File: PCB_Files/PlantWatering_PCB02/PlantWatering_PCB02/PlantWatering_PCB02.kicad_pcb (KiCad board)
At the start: 4 copper layers, 109 x 55.5 mm, 62 parts, among them J1 Battery connection, J10 I2C Pins, J11 I2C Pins, J2 AnalogSignals, J3 32KHZ/SQW, J4 Solar Panel, J5 Power output, J6 Signal Sockets, J7 Connector to other Board, J8 I2C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

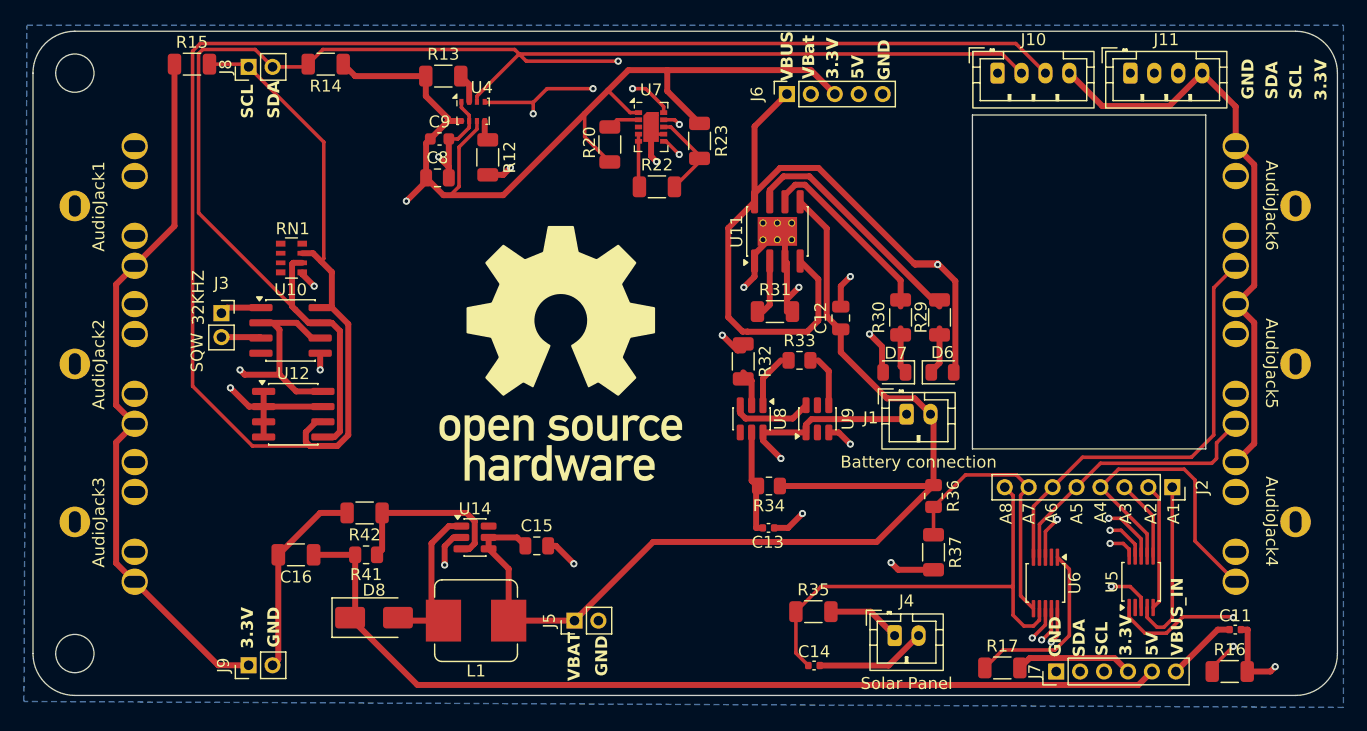
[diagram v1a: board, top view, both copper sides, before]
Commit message: modified PCB02 for 2Layer board in order to save money
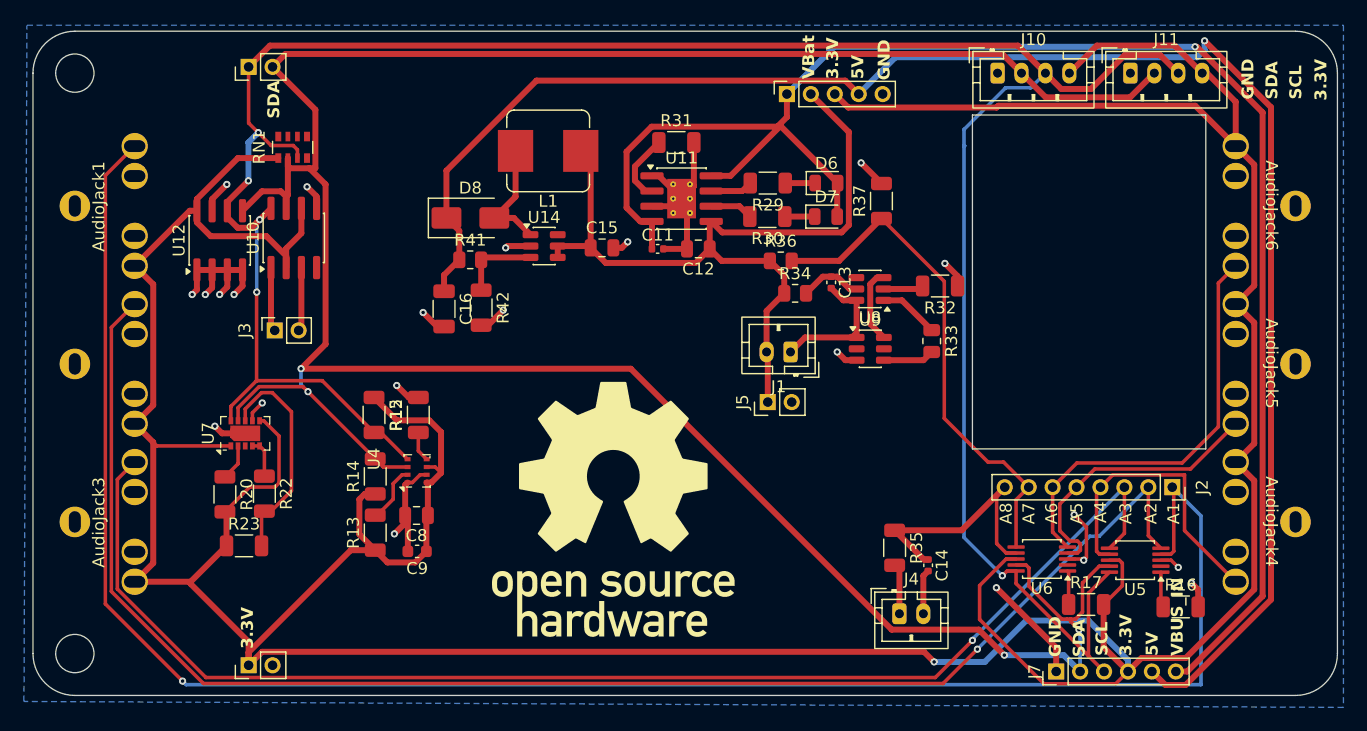
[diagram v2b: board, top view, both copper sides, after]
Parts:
- moved C11 57.8 mm to (98.7, 92.7)
- moved R23 50.9 mm to (64.1, 117.5), turned to 0 degrees
- moved R20 43.5 mm to (62.5, 113.2)
- moved U7 42.5 mm to (64.2, 108.1), turned to 90 degrees
- moved R22 41.6 mm to (65.8, 113.1), turned to -90 degrees
- moved L1 39.7 mm to (89.5, 84.5)
- moved R13 38.6 mm to (75.1, 116.4), turned to 90 degrees
- moved R14 34.7 mm to (75.1, 111.7), turned to 90 degrees
- moved C9 34.5 mm to (78.6, 118.0), turned to 180 degrees
- moved D8 34.4 mm to (83.0, 90.1)
- moved R15 33.0 mm to (75.0, 106.6), turned to -90 degrees
- moved U4 30.4 mm to (78.6, 111.2), turned to 90 degrees
- moved R37 29.7 mm to (117.4, 88.7), turned to 90 degrees
- moved C8 28.3 mm to (78.5, 115.0), turned to 180 degrees
- moved R41 26.1 mm to (83.0, 93.6)
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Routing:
- net /SCL: track 293.7 -> 205.6 mm
- net /VBat: track 124.5 -> 68.4 mm
- net /Analog1: track 125.1 -> 157.7 mm, vias 0 -> 1
- net /Analog2: track 105.7 -> 127.0 mm, vias 0 -> 1
- net /Analog7: track 22.7 -> 42.7 mm
- net /SDA: track 248.2 -> 230.9 mm
- net /Analog8: track 38.7 -> 21.4 mm
- net Net-(U11-~{CHRG}): track 20.1 -> 3.54 mm
- net /Analog3: track 95.1 -> 110.7 mm, vias 0 -> 1
- net +3.3V: track 384.0 -> 369.3 mm, vias 6 -> 1
- net GND: track 101.9 -> 88.0 mm, vias 16 -> 22
- net Net-(U5-ADDR): track 15.9 -> 2.98 mm, vias 2 -> 0
- net Net-(U11-~{STDBY}): track 16.1 -> 3.58 mm
- net Net-(U6-ADDR): track 15.1 -> 2.84 mm
- net /S1: track 24.0 -> 11.9 mm, vias 2 -> 0
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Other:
- copper layers 4 -> 2
- board text removed: "32KHZ"
- board text removed: "@benedikt314159"
- board text removed: "SQW"
- board text removed: "VBAT"
- board text removed: "VBUS"

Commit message: update PDF and added labels to PCB02
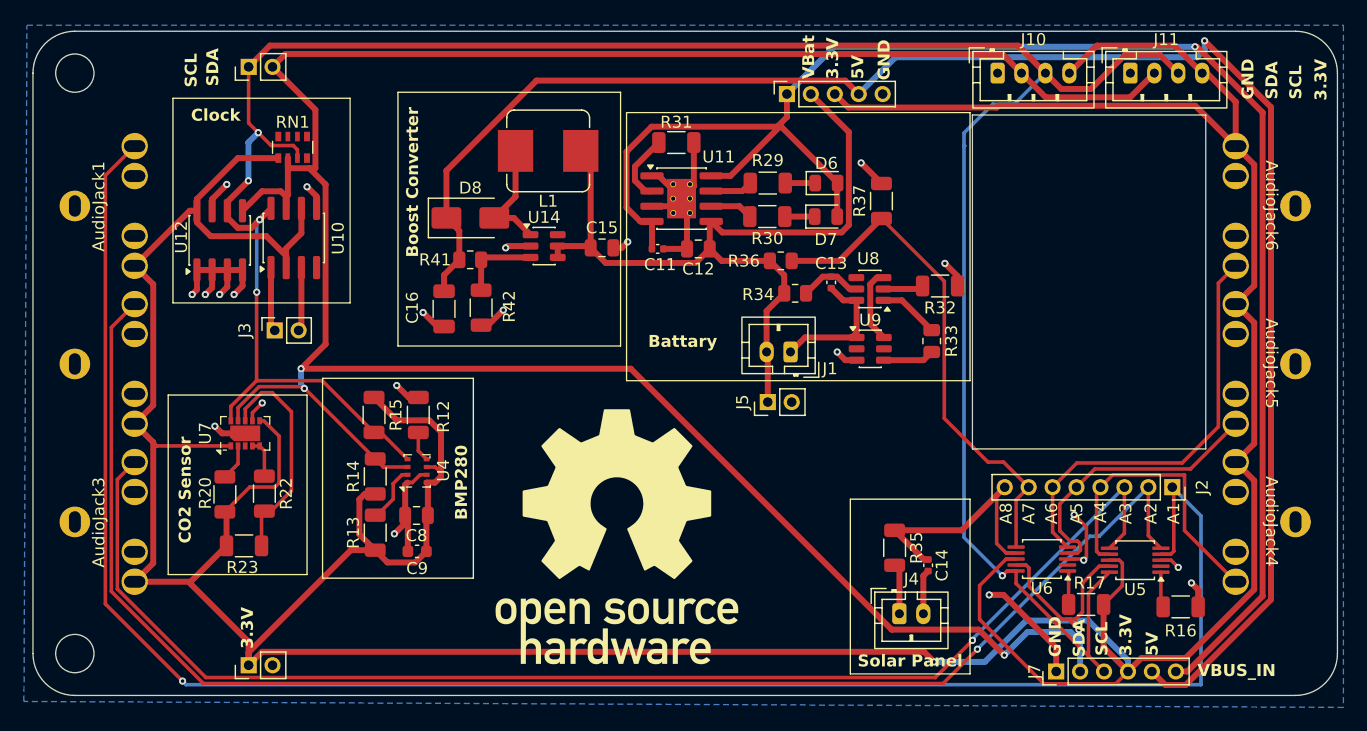
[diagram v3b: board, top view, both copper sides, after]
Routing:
- net /SDA: track 230.9 -> 234.1 mm
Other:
- board text added: "Battary"
- board text added: "Boost Converter"
- board text added: "CO2 Sensor"
- board text added: "Clock"
- board text added: "Solar Panel"
